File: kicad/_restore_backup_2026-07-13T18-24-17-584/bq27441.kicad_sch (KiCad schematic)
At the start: 7 parts, among them U2 TPS22917DBV

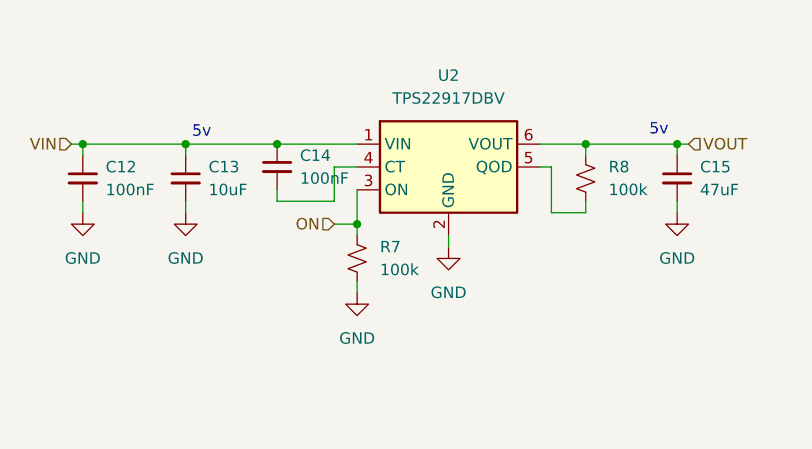
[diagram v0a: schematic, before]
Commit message: finished schematic and started pcb routing
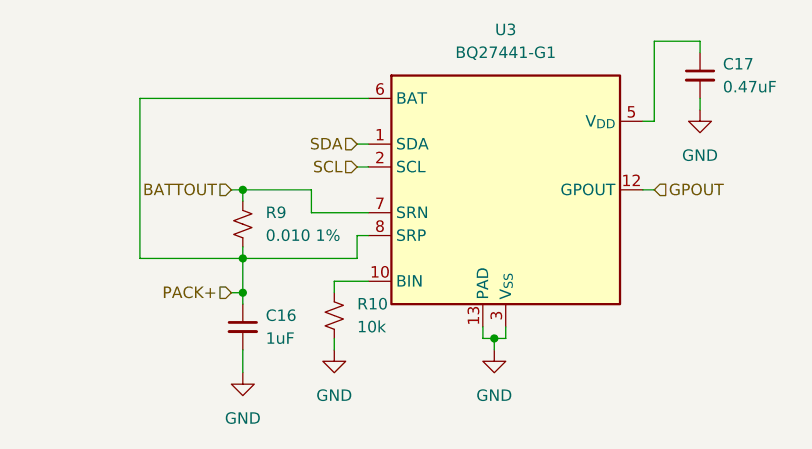
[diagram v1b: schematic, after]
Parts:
- removed C12: 100nF, Capacitor_SMD:C_0805_2012Metric, symbol Device:C_Small
- removed C13: 10uF, Capacitor_SMD:C_0805_2012Metric, symbol Device:C_Small
- removed C14: 100nF, Capacitor_SMD:C_0402_1005Metric, symbol Device:C_Small
- removed C15: 47uF, Capacitor_SMD:C_0805_2012Metric, symbol Device:C_Small
- removed R7: 100k, Resistor_SMD:R_0402_1005Metric, symbol Device:R_Small_US
- removed R8: 100k, Resistor_SMD:R_0603_1608Metric, symbol Device:R_Small_US
- removed U2: TPS22917DBV, Package_TO_SOT_SMD:SOT-23-6, symbol Power_Management:TPS22917DBV
- added C16: 1uF, symbol Device:C_Small
- added C17: 0.47uF, symbol Device:C_Small
- added R10: 10k, symbol Device:R_Small_US
- added R9: 0.010 1%, symbol Device:R_Small_US
- added U3: BQ27441-G1, Package_SON:Texas_S-PDSO-N12, symbol Battery_Management:BQ27441-G1
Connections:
- net GND: now also C16.2, C17.2, R10.2, U3.13 (PAD), U3.3 (V_{SS})
- new net: R10.1, U3.10 (BIN)
- new net: C17.1, U3.5 (V_{DD})
- new net BATTOUT: R9.1, U3.7 (SRN)
- new net GPOUT: U3.12 (GPOUT)
- new net PACK+: C16.1, R9.2, U3.6 (BAT), U3.8 (SRP)
- new net SCL: U3.2 (SCL)
- new net SDA: U3.1 (SDA)
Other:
- note removed: "5v"
